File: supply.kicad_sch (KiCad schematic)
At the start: 156 parts, among them J7 BarrelJack_3167288, J8 JST_SH_1x4_BM04B-SRSS-TB-LF-SN, Q12 SI7613DN-T1-GE3, Q13 SI7613DN-T1-GE3, Q14 BSS138PW, Q15 BSS138PW, Q16 BSS138PW, Q17 BSS138PW, SW4 SW_CVS-08TB, SW5 SW_KMR211NGLFS_SMD, U17 LTC4412IS6, U18 LTC4412IS6, U19 MPM54304GMN, U20 MPM54304GMN, U21 NCP718BSN330T1G, U22 MAX16150A_SOT, U25 PAC1954T-E_VQFN, U26 MAX812REUS+T, U27 MP8869S, U28 XC6230H001ER-G, U29 MCP4726A0T-E_MAY, U30 PAC1954T-E_VQFN, U31 LM3880

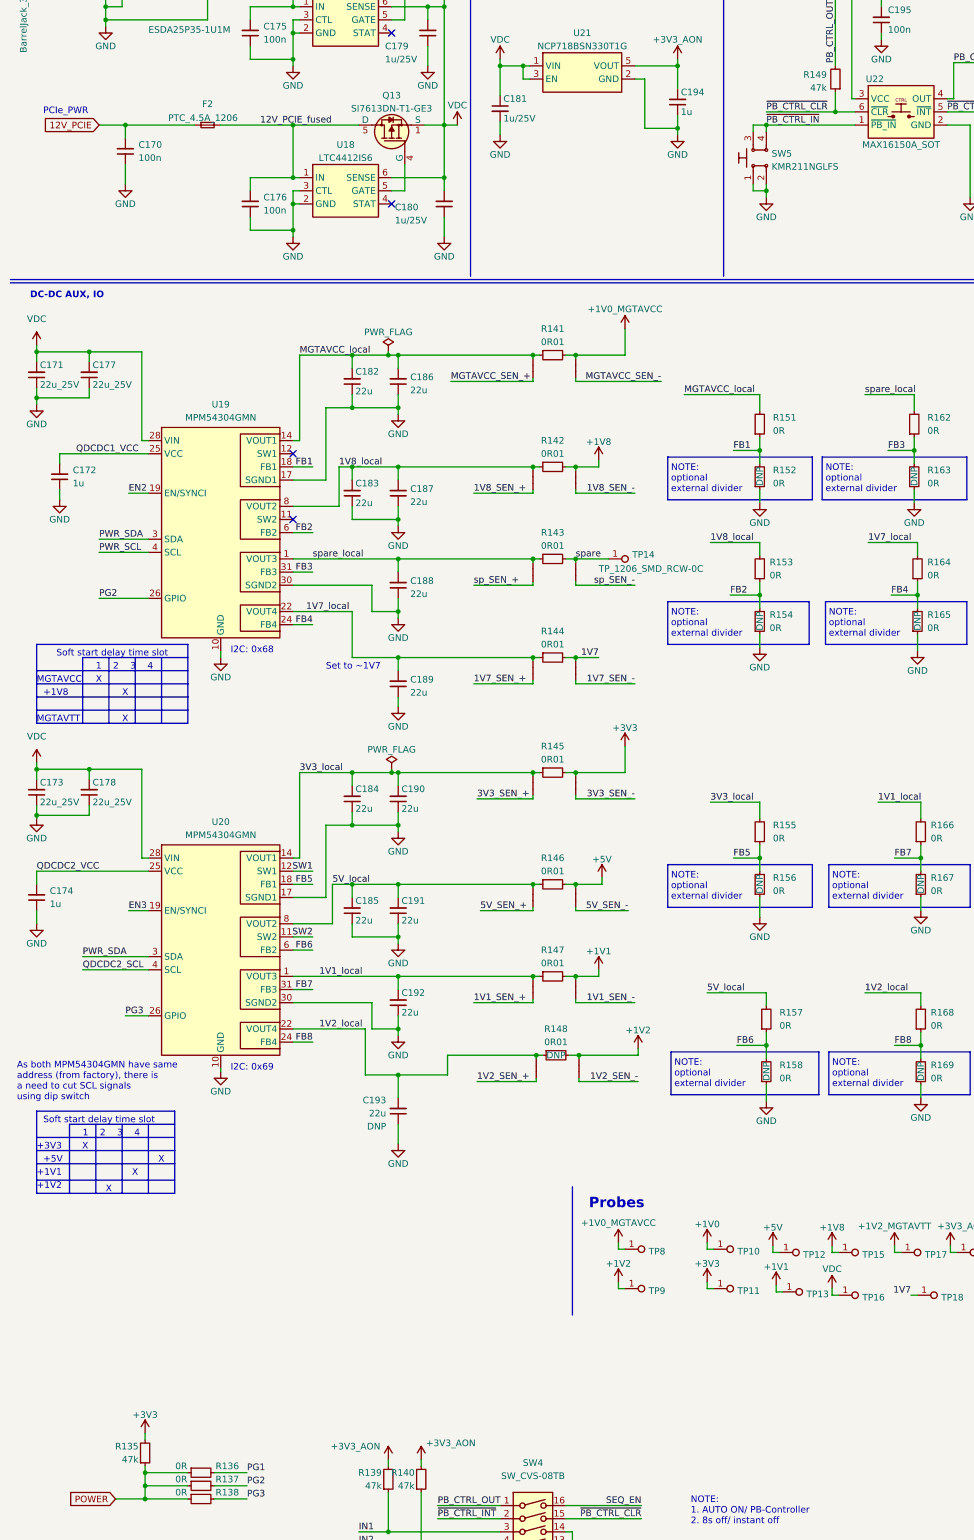
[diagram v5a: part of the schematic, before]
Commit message: Finish creating hierarchical buses and structure, start reconnecting signals
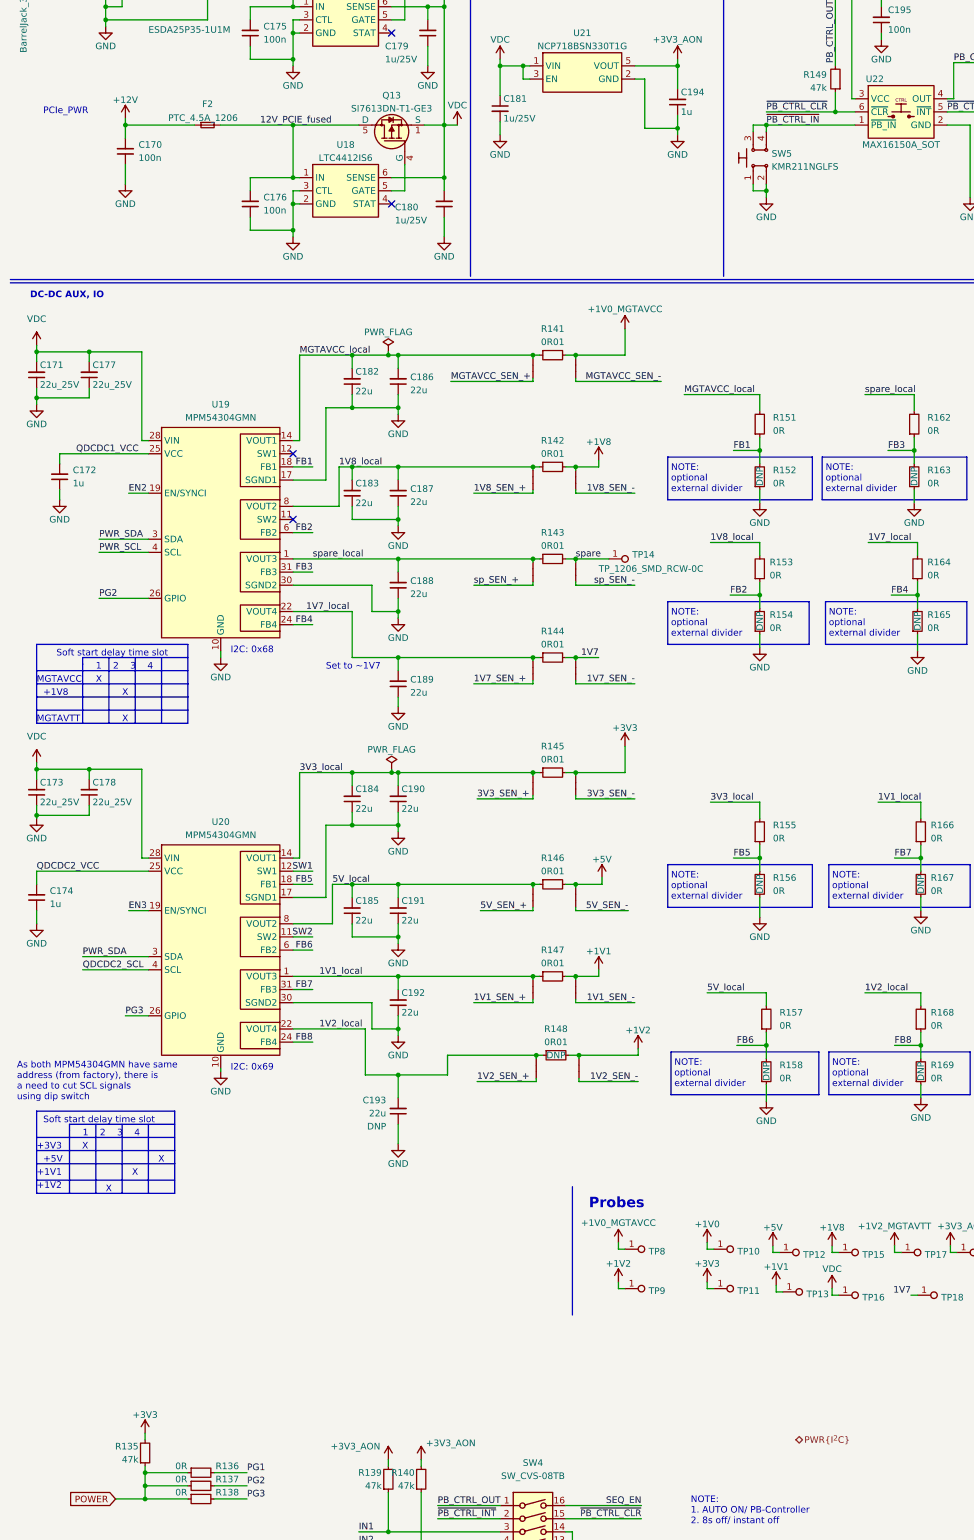
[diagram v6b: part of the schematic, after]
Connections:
- net 12V_PCIE renamed +12V
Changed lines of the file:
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@@
     (stroke (width 0) (type default) (color 0 0 0 0))
   )
-  (wire (pts (xy 29.21 55.245) (xy 34.29 55.245))
-    (stroke (width 0) (type default) (color 0 0 0 0))
-  )
   (wire (pts (xy 193.04 50.165) (xy 194.31 50.165))
     (stroke (width 0) (type default) (color 0 0 0 0))
@@
     (stroke (width 0) (type default) (color 0 0 0 0))
   )
+  (wire (pts (xy 34.29 53.975) (xy 34.29 55.245))
+    (stroke (width 0) (type default) (color 0 0 0 0))
+  )
   (wire (pts (xy 66.675 133.985) (xy 70.485 133.985))
     (stroke (width 0) (type default) (color 0 0 0 0))
@@
     )
   )
-  (global_label "12V_PCIE" (shape input) (at 29.21 55.245 180) (fields_autoplaced)
-    (effects (font (size 1.27 1.27)) (justify right))
-    (property "Intersheet References" "${INTERSHEET_REFS}" (id 0) (at 18.1168 55.1656 0)
-      (effects (font (size 1.27 1.27)) (justify right) hide)
-    )
-  )
   (global_label "POWER" (shape input) (at 32.385 320.675 180) (fields_autoplaced)
     (effects (font (size 1.27 1.27)) (justify right))
@@
     )
   )
+  (hierarchical_label "PWR{I^{2}C}" (shape bidirectional) (at 163.83 309.245 0)
+    (effects (font (size 1.27 1.27)) (justify left))
+  )
   (symbol (lib_id "sodimm-ddr5-tester:TP_1mm_SMD") (at 160.655 273.05 0) (unit 1)
     (in_bom yes) (on_board yes) (fields_autoplaced)
@@
     )
     (pin "1")
+  )
+  (symbol (lib_id "antmicropower:+12V") (at 34.29 53.975 0) (unit 1)
+    (in_bom yes) (on_board yes) (fields_autoplaced)
+    (property "Reference" "#PWR?" (id 0) (at 34.29 57.785 0)
+      (effects (font (size 1.27 1.27)) hide)
+    )
+    (property "Value" "+12V" (id 1) (at 34.29 50.3992 0))
+    (property "Footprint" "" (id 2) (at 34.29 53.975 0)
+      (effects (font (size 1.27 1.27)) hide)
+    )
+    (property "Datasheet" "" (id 3) (at 34.29 53.975 0)
+      (effects (font (size 1.27 1.27)) hide)
+    )
+    (pin "1")
